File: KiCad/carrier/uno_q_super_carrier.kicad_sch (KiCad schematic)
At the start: 0 parts

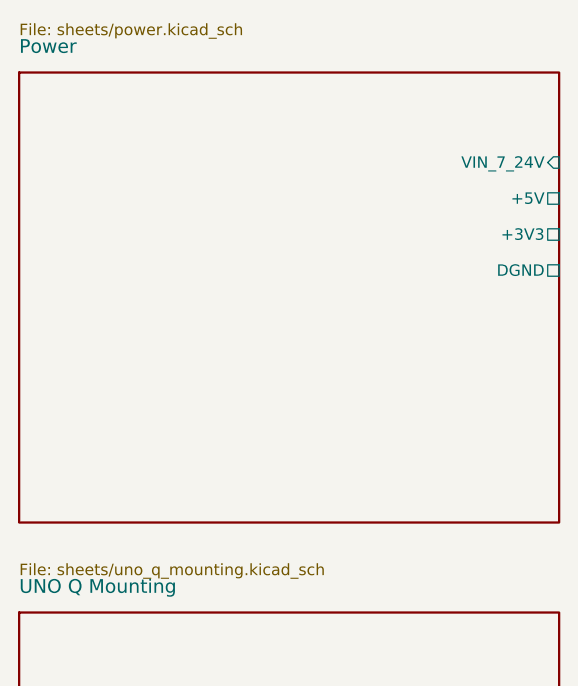
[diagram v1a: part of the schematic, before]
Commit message: Use only standard KiCad libraries - remove HybotixParts dependency
Replaced all custom HybotixParts component references with standard KiCad libraries:
- BarrelJack_5V → Connector:Conn_01x02_Pin
- AMS1117-3.3 → Regulator_Linear:AMS1117-3.3
- ESP32-S3-WROOM-1-N16R8 → Module:ESP32-WROOM-32
- SN74HCT245PW → Logic_Inverter:SN74HCT245
- ES8388 → Audio:ES8388
- USB-C → Connector:USB_C_Receptacle_usb2.0
- FPC connectors → standard Connector parts
- All others mapped to nearest KiCad library equivalent

Removed embedded symbols section - all components now use standard KiCad built-in libraries.

All 16 schematics verified to parse correctly.
No external dependencies - ready to open in KiCad 10.0.2 on any machine.
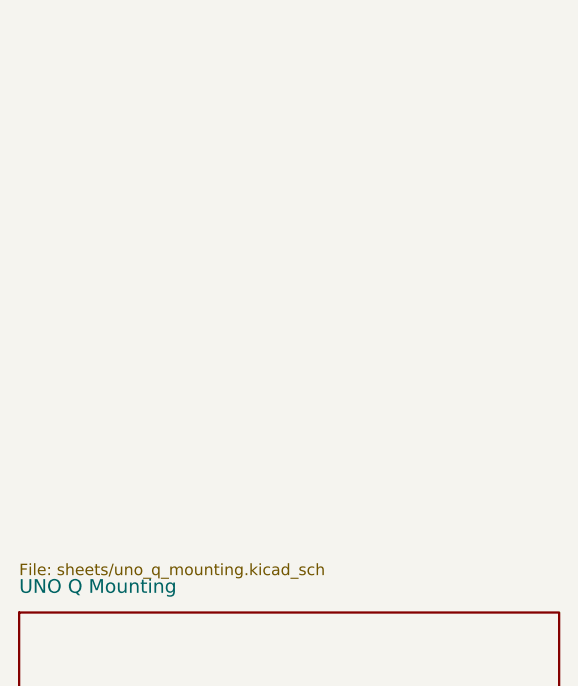
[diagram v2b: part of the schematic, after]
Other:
- removed sheet Power
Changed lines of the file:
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@@
-  )
-  (sheet
-    (at 20 30)
-    (size 60 50)
-    (stroke (width 0.254) (type default))
-    (fill (type color) (color 255 255 204 0.3))
-    (property "Sheet name" "Power"
-      (at 20 28 0)
-      (effects (font (size 1.524 1.524)) (justify left bottom))
-    )
-    (property "Sheet file" "sheets/power.kicad_sch"
-      (at 20 26 0)
-      (effects (font (size 1.27 1.27)) (justify left bottom))
-    )
-    (pin "VIN_7_24V" input
-      (at 80 40 0)
-      (effects (font (size 1.27 1.27)))
-    )
-    (pin "+5V" power_out
-      (at 80 44 0)
-      (effects (font (size 1.27 1.27)))
-    )
-    (pin "+3V3" power_out
-      (at 80 48 0)
-      (effects (font (size 1.27 1.27)))
-    )
-    (pin "DGND" power_out
-      (at 80 52 0)
-      (effects (font (size 1.27 1.27)))
-    )
-    (instances
-      (project "uno_q_super_carrier"
-        (path "/a7d62ed3-8e95-4e64-b6df-722c91664a1a"
-          (page "2")
-        )
-      )
-    )
   )
   (sheet
